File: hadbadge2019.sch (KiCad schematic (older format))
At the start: 0 parts

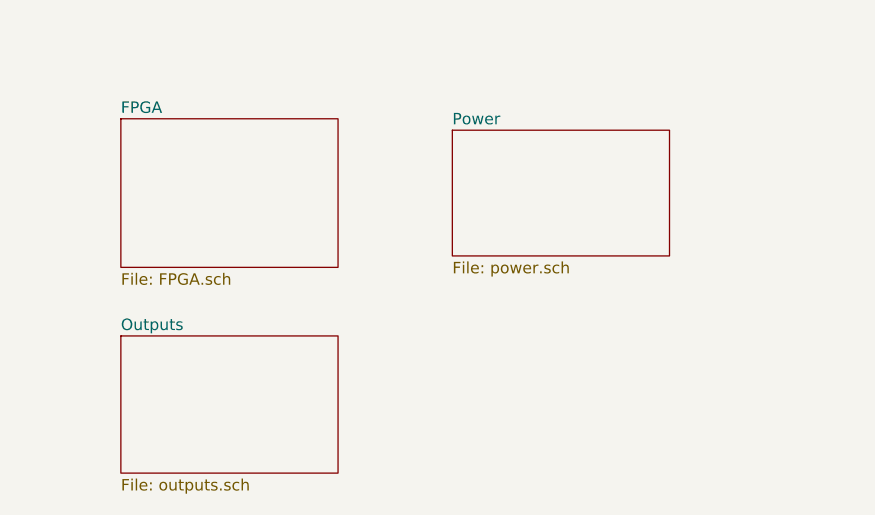
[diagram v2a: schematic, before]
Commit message: Note oopsie in scl/sda
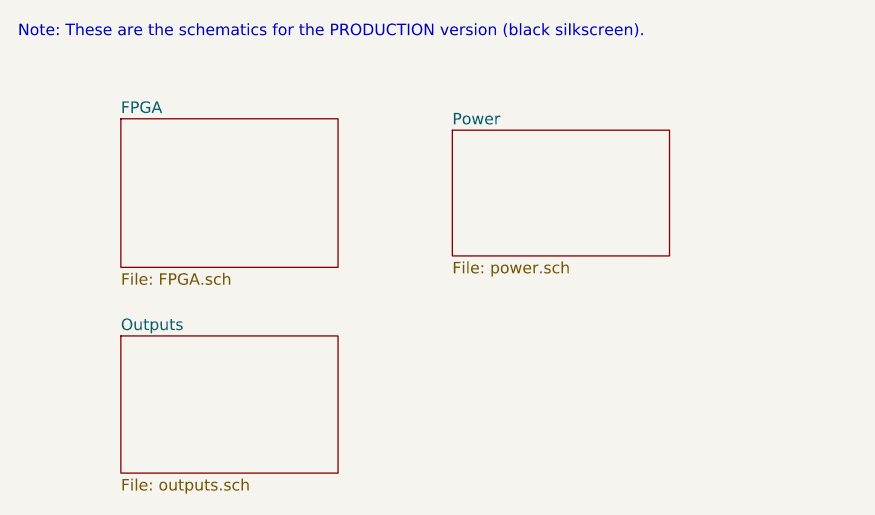
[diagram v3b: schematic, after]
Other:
- note added: "Note: These are the schematics for the PRODUCTION version (black silkscreen)."
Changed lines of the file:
@@
 F1 "outputs.sch" 50
 $EndSheet
+Text Notes 2000 1150 0    50   ~ 0
+Note: These are the schematics for the PRODUCTION version (black silkscreen).
 $EndSCHEMATC
